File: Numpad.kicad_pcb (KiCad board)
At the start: 2 copper layers, 82.6 x 127 mm, 68 parts, among them J1 SWD, J2 USB_C_Receptacle_USB2.0, U1 SRV05-4, U2 STM32F103C8Tx, U3 XC6206PxxxMR, Y1 8MHz

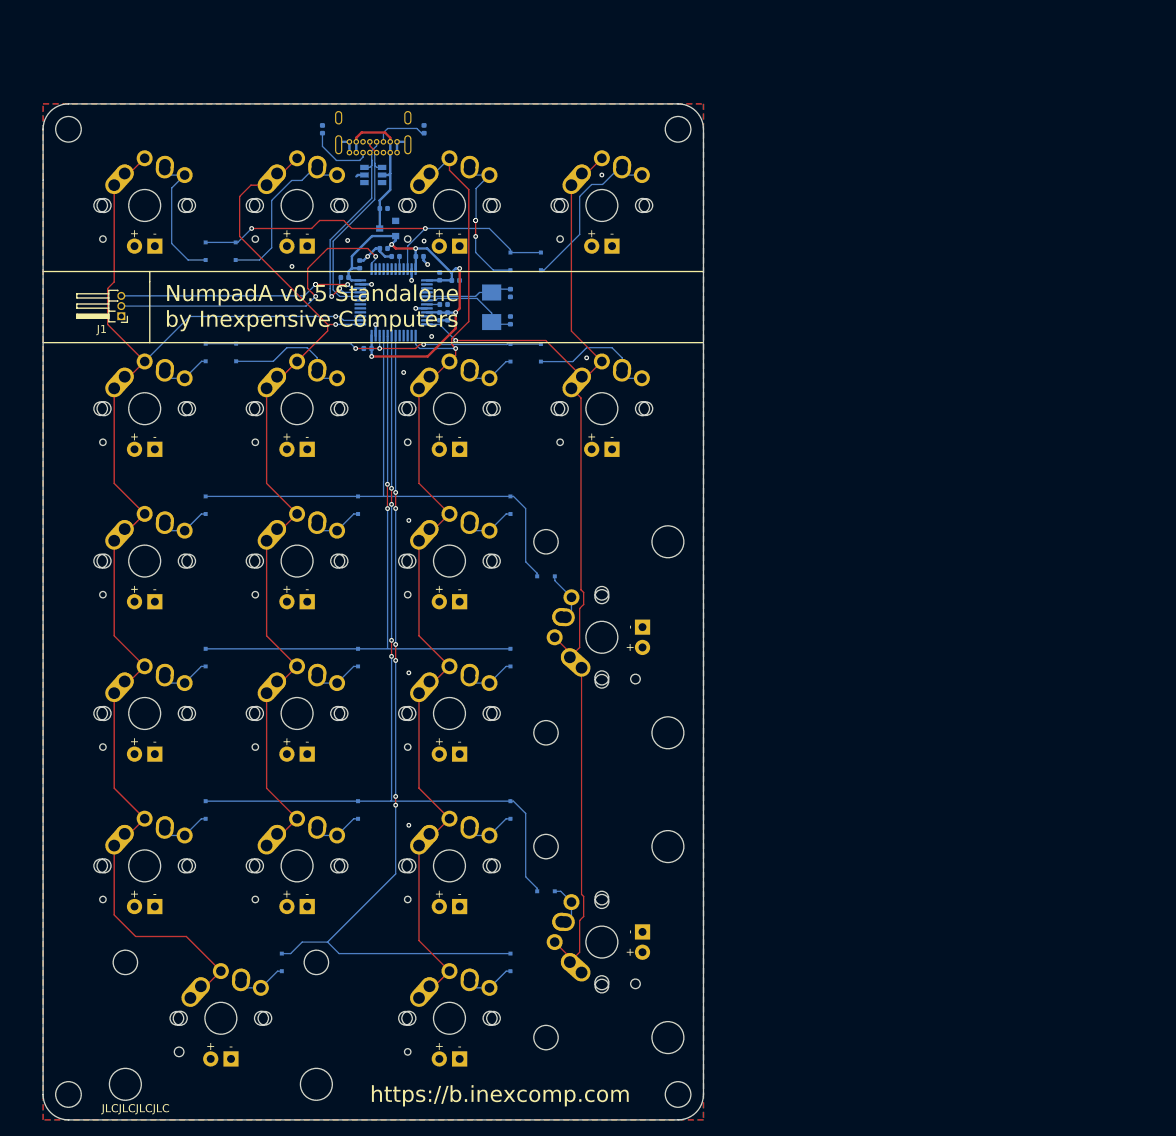
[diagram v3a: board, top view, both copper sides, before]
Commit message: Fixed header footprint
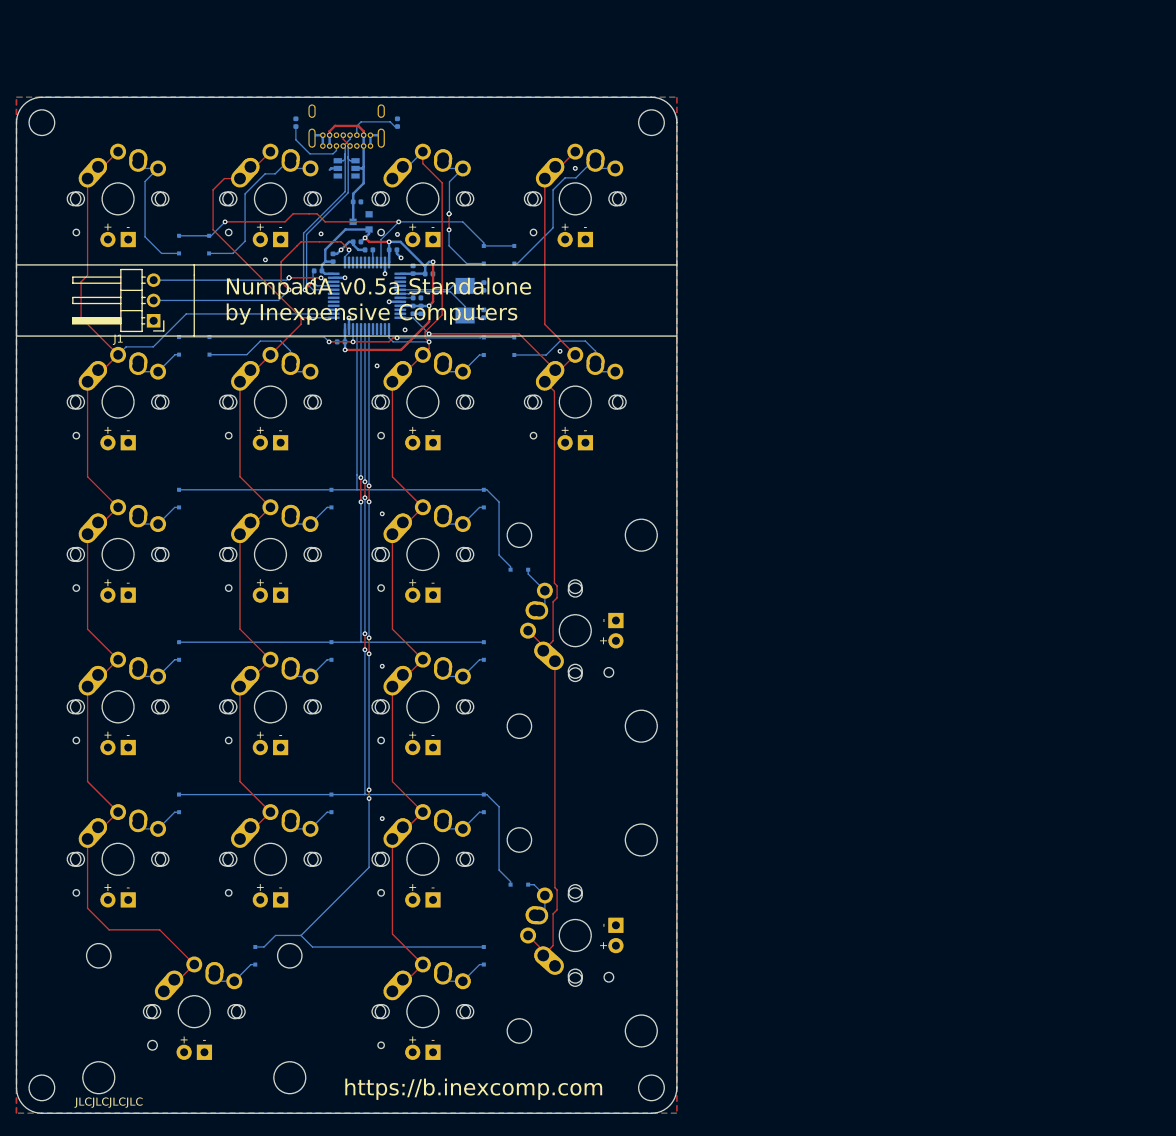
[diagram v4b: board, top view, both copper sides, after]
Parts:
- J1: footprint Connector_PinHeader_1.27mm:PinHeader_1x03_P1.27mm_Horizontal -> Connector_PinHeader_2.54mm:PinHeader_1x03_P2.54mm_Horizontal
- moved J1 4.08 mm to (55.2, 66.0)
- moved D_SLASH1 3.43 mm to (62.2, 69.2)
- moved C2 3.43 mm to (78.7, 68.7)
- moved C5 3.43 mm to (88.7, 64.7)
- moved C6 3.43 mm to (87.7, 64.7)
- moved C9 3.43 mm to (96.5, 65.2)
- moved D_0 3.43 mm to (67.9, 145.4)
- moved D_5 3.43 mm to (77.5, 107.3)
- moved D_6 3.43 mm to (96.5, 107.3)
- moved D_8 3.43 mm to (77.5, 88.3)
- moved D_9 3.43 mm to (96.5, 88.3)
- moved D_DOT1 3.43 mm to (96.5, 145.4)
- moved D_ENTER1 3.43 mm to (101.0, 136.5)
- moved D_MINUS1 3.43 mm to (100.3, 69.2)
- moved D_PLUS1 3.43 mm to (101.0, 97.2)
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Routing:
- net SWDIO: track 30.7 -> 22.8 mm
- net SWDCLK: track 40.4 -> 33.1 mm
- net col1: track 150.2 -> 149.8 mm, vias 1 -> 0
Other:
- board text added: "NumpadA v0.5a Standalone by Inexpensive Computers"
- board text removed: "NumpadA v0.5 Standalone by Inexpensive Computers"

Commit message: some changes; added license
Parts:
- removed J1: SWD, Connector_PinHeader_2.54mm:PinHeader_1x03_P2.54mm_Horizontal
- added GND1: TestPoint, TestPoint:TestPoint_Pad_D2.0mm, B.Cu at (65.1, 63.4)
- added SCK1: TestPoint, TestPoint:TestPoint_Pad_D2.0mm, B.Cu at (69.2, 63.4)
- added SIO1: TestPoint, TestPoint:TestPoint_Pad_D2.0mm, B.Cu at (73.2, 63.4)
- D_0, D_1, D_2, D_3, D_4, D_5, D_6, D_7, D_8, D_9, D_BKSP1, D_DOT1, D_ENTER1, D_ESC1, D_FN1, D_MINUS1, D_NUMLK1, D_PLUS1, D_SLASH1, D_STAR1, D_TAB1: value 1N4148 -> 1N4148WS; footprint Diode_SMD:D_SOD-323F -> Diode_SMD:D_SOD-323
- SW_0, SW_1, SW_2, SW_3, SW_4, SW_5, SW_6, SW_7, SW_8, SW_9, SW_BKSP1, SW_DOT1, SW_ENTER1, SW_ESC1, SW_FN1, SW_MINUS1, SW_NUMLK1, SW_PLUS1, SW_SLASH1, SW_STAR1, SW_TAB1: value SW_Push -> MX-LED
- moved C8 0.86 mm to (97.4, 61.6)
- moved D_0 0.86 mm to (68.8, 145.3)
- moved D_3 0.86 mm to (97.4, 126.2)
- moved D_DOT1 0.86 mm to (97.4, 145.3)
- moved D_STAR1 0.86 mm to (97.4, 69.1)
- moved H2 0.86 mm to (118.3, 41.1)
- moved H4 0.86 mm to (118.3, 161.8)
- moved R2 0.86 mm to (73.9, 41.1)
- moved R3 0.86 mm to (86.6, 41.1)
- moved SW_2 0.86 mm to (70.7, 133.2)
- moved SW_3 0.86 mm to (89.8, 133.2)
- moved SW_SLASH1 0.86 mm to (70.7, 76.0)
- moved SW_STAR1 0.86 mm to (89.8, 76.0)
- moved D_FN1 0.86 mm to (97.4, 57.6)
- moved R1 0.86 mm to (83.0, 57.0)
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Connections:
- SW_0 pad 3: (no net) -> LED_PWR
- SW_0 pad 4: (no net) -> GND
- SW_1 pad 3: (no net) -> LED_PWR
- SW_1 pad 4: (no net) -> GND
- SW_2 pad 3: (no net) -> LED_PWR
- SW_2 pad 4: (no net) -> GND
- SW_3 pad 3: (no net) -> LED_PWR
- SW_3 pad 4: (no net) -> GND
- SW_4 pad 3: (no net) -> LED_PWR
- SW_4 pad 4: (no net) -> GND
- SW_5 pad 3: (no net) -> LED_PWR
- SW_5 pad 4: (no net) -> GND
- SW_6 pad 3: (no net) -> LED_PWR
- SW_6 pad 4: (no net) -> GND
- SW_7 pad 3: (no net) -> LED_PWR
- SW_7 pad 4: (no net) -> GND
- SW_8 pad 3: (no net) -> LED_PWR
- SW_8 pad 4: (no net) -> GND
- SW_9 pad 3: (no net) -> LED_PWR
- SW_9 pad 4: (no net) -> GND
- SW_BKSP1 pad 3: (no net) -> LED_PWR
- SW_BKSP1 pad 4: (no net) -> GND
- SW_DOT1 pad 3: (no net) -> LED_PWR
- SW_DOT1 pad 4: (no net) -> GND
- SW_ENTER1 pad 3: (no net) -> LED_PWR
- SW_ENTER1 pad 4: (no net) -> GND
- SW_ESC1 pad 3: (no net) -> LED_PWR
- SW_ESC1 pad 4: (no net) -> GND
- SW_FN1 pad 3: (no net) -> LED_PWR
- SW_FN1 pad 4: (no net) -> GND
- SW_MINUS1 pad 3: (no net) -> LED_PWR
- SW_MINUS1 pad 4: (no net) -> GND
- SW_NUMLK1 pad 3: (no net) -> LED_PWR
- SW_NUMLK1 pad 4: (no net) -> GND
- SW_PLUS1 pad 3: (no net) -> LED_PWR
- SW_PLUS1 pad 4: (no net) -> GND
- SW_SLASH1 pad 3: (no net) -> LED_PWR
- SW_SLASH1 pad 4: (no net) -> GND
- SW_STAR1 pad 3: (no net) -> LED_PWR
- SW_STAR1 pad 4: (no net) -> GND
- SW_TAB1 pad 3: (no net) -> LED_PWR
- SW_TAB1 pad 4: (no net) -> GND
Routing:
- net SWDIO: track 22.8 -> 7.49 mm, vias 3 -> 2
- net SWDCLK: track 33.1 -> 18.3 mm
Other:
- outline, holes or cut-outs redrawn
- board text added: "NumpadA v0.6 Standalone by Inexpensive Computers"
- board text removed: "NumpadA v0.5a Standalone by Inexpensive Computers"

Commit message: v0.9pre
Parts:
- removed C1, C2, C3, C4, C6: 100nf, Capacitor_SMD:C_0402_1005Metric
- removed C5: 1uf, Capacitor_SMD:C_0402_1005Metric
- removed D_0, D_1, D_2, D_3, D_4, D_5, D_6, D_7, D_8, D_9, D_BKSP1, D_DOT1, D_ENTER1, D_ESC1, D_FN1, D_MINUS1, D_NUMLK1, D_PLUS1, D_SLASH1, D_STAR1, D_TAB1: 1N4148WS, Diode_SMD:D_SOD-323
- removed J2: USB_C_Receptacle_USB2.0, Connector_USB:USB_C_Receptacle_GCT_USB4085
- removed R4: 1.5K, Resistor_SMD:R_0402_1005Metric
- added C13: 20pf, Capacitor_SMD:C_0402_1005Metric, B.Cu at (80.6, 66.7)
- added C14: 100nf, Capacitor_SMD:C_0402_1005Metric, B.Cu at (81.3, 61.3)
- added C15: 100nf, Capacitor_SMD:C_0402_1005Metric, B.Cu at (87.6, 58.4)
- added C16: 1uf, Capacitor_SMD:C_0402_1005Metric, B.Cu at (79.4, 61.3)
- added C17: 100nf, Capacitor_SMD:C_0402_1005Metric, B.Cu at (80.3, 61.3)
- added C18: 100nf, Capacitor_SMD:C_0402_1005Metric, B.Cu at (77.5, 49.5)
- added D1: WS2813, LED_SMD:LED_WS2812_PLCC6_5.0x5.0mm_P1.6mm, B.Cu at (62.9, 53.3)
- added D10: BAT54C, Package_TO_SOT_SMD:SOT-23, B.Cu at (62.9, 101.0)
- added D11: BAT54C, Package_TO_SOT_SMD:SOT-23, B.Cu at (62.9, 115.6)
- added D12: BAT54C, Package_TO_SOT_SMD:SOT-23, B.Cu at (81.9, 139.7)
- added D13: BAT54C, Package_TO_SOT_SMD:SOT-23, B.Cu at (101.0, 43.8)
- added D14: BAT54C, Package_TO_SOT_SMD:SOT-23, B.Cu at (101.0, 60.3)
- added D15: BAT54C, Package_TO_SOT_SMD:SOT-23, B.Cu at (101.0, 77.5)
- added D16: BAT54C, Package_TO_SOT_SMD:SOT-23, B.Cu at (101.0, 101.0)
- added D17: BAT54C, Package_TO_SOT_SMD:SOT-23, B.Cu at (101.0, 115.6)
- added D2: WS2813, LED_SMD:LED_WS2812_PLCC6_5.0x5.0mm_P1.6mm, B.Cu at (99.1, 53.3)
- added D3: WS2813, LED_SMD:LED_WS2812_PLCC6_5.0x5.0mm_P1.6mm, B.Cu at (62.9, 92.7)
- added D4: WS2813, LED_SMD:LED_WS2812_PLCC6_5.0x5.0mm_P1.6mm, B.Cu at (99.1, 92.7)
- added D5: WS2813, LED_SMD:LED_WS2812_PLCC6_5.0x5.0mm_P1.6mm, B.Cu at (62.9, 130.2)
- added D6: WS2813, LED_SMD:LED_WS2812_PLCC6_5.0x5.0mm_P1.6mm, B.Cu at (99.1, 130.2)
- added D7: BAT54C, Package_TO_SOT_SMD:SOT-23, B.Cu at (62.9, 43.8)
- added D8: BAT54C, Package_TO_SOT_SMD:SOT-23, B.Cu at (62.9, 61.6)
- added D9: BAT54C, Package_TO_SOT_SMD:SOT-23, B.Cu at (62.9, 77.5)
- added F1: SMD0805P050TF, Fuse:Fuse_0805_2012Metric_Castellated, B.Cu at (83.8, 38.7)
- added G***: LOGO, Logo:inexcomplogo1, F.Cu at (53.3, 52.7)
- added G***: LOGO, Logo:OSHWMark, F.Cu at (109.2, 52.7)
- added J1: USB_C_Receptacle_USB2.0, Connector_USB:USB_C_Receptacle_HRO_TYPE-C-31-M-12, B.Cu at (81.9, 31.1)
- added Q1: AO3401A, Package_TO_SOT_SMD:SOT-23, B.Cu at (90.2, 51.4)
- added R11: 10k, Resistor_SMD:R_0402_1005Metric, B.Cu at (88.3, 55.2)
- added R12: 1.5K, Resistor_SMD:R_0402_1005Metric, B.Cu at (83.8, 46.0)
- added R13: 5.1K, Resistor_SMD:R_0402_1005Metric, B.Cu at (89.2, 34.6)
- added R14: 5.1K, Resistor_SMD:R_0402_1005Metric, B.Cu at (87.8, 34.6)
- C10, C7: value 100nf -> 1uf
- C11: value 1uf -> 100nf
- C12: value 1uf -> 20pf
- C8, C9: value 20pf -> 100nf
- R1: value 10k -> 10K
- R2: value 5.1K -> 150R
- R3: value 5.1K -> 1M
- SW_0, SW_ENTER1, SW_PLUS1: footprint Keebio-Parts:MX-Alps-Choc-2U -> Keebio-Parts:MX-Alps-Choc-2U-StabFlip
- U1: value SRV05-4 -> STM32F103C8Tx; footprint Package_TO_SOT_SMD:SOT-23-6 -> Package_QFP:LQFP-48_7x7mm_P0.5mm
- U2: value STM32F103C8Tx -> XC6206PxxxMR; footprint Package_QFP:LQFP-48_7x7mm_P0.5mm -> Package_TO_SOT_SMD:SOT-23
- U3: value XC6206PxxxMR -> SRV05-4; footprint Package_TO_SOT_SMD:SOT-23 -> Package_TO_SOT_SMD:SOT-23-6
- moved H3 159.9 mm to (139.4, 34.9)
- moved H4 120.8 mm to (139.4, 42.9)
- moved H1 89.5 mm to (131.4, 34.9)
- moved C9 25.0 mm to (76.8, 50.8), turned to 180 degrees
- moved R2 21.3 mm to (90.8, 54.0), turned to 180 degrees
- moved SIO1 18.4 mm to (57.8, 53.3), turned to 270 degrees
- moved U2 17.4 mm to (86.4, 45.7)
- moved C7 17.0 mm to (86.4, 43.5)
- moved C10 15.1 mm to (87.6, 47.9)
- moved GND1 15.1 mm to (57.8, 50.2), turned to 270 degrees
- moved R3 14.6 mm to (72.4, 37.5), turned to 180 degrees
- moved SCK1 13.3 mm to (57.8, 56.5), turned to 270 degrees
- moved H2 13.2 mm to (131.4, 42.9)
- moved Y1 13.1 mm to (81.9, 64.1), turned to 0 degrees
- moved C8 11.2 mm to (86.4, 59.7), turned to 180 degrees
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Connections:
- net LED_PWR renamed LED_MATRIX
- C10 pad 1: NRST -> VBAT
- C11 pad 2: +5V -> VBAT
- C12 pad 1: VBAT -> PD0
- C7 pad 2: VBAT -> +5V
- C8 pad 1: PD0 -> GND
- C8 pad 2: GND -> VBAT
- C9 pad 1: PD1 -> GND
- C9 pad 2: GND -> VBAT
- R1 pad 1: BOOT0 -> +5V
- R1 pad 2: GND -> LED_CONTROL
- R2 pad 1: /CC1 -> Net-(Q1-Pad1)
- R2 pad 2: GND -> LED_CONTROL
- R3 pad 1: GND -> Net-(J1-PadS1)
- R3 pad 2: /CC2 -> GND
- U1 pad 1: (no net) -> VBAT
- U1 pad 2: GND -> (no net)
- U1 pad 3: DA+ -> (no net)
- U1 pad 4: DA- -> (no net)
- U1 pad 5: +5V -> PD0
- U1 pad 6: (no net) -> PD1
- U2 pad 1: VBAT -> GND
- U2 pad 2: (no net) -> VBAT
- U2 pad 3: (no net) -> +5V
- U3 pad 1: GND -> (no net)
- U3 pad 2: VBAT -> GND
- U3 pad 3: +5V -> DA-
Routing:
- net GND: track 19.9 -> 541.1 mm, vias 16 -> 92
- net LED_MATRIX: track 0.00 -> 461.7 mm, vias 0 -> 26
- net +5V: track 19.6 -> 224.8 mm, vias 0 -> 15
- net Net-(D2-Pad4): track 0.00 -> 99.5 mm, vias 0 -> 8
- net Net-(D2-Pad6): track 0.00 -> 98.1 mm, vias 0 -> 10
- net Net-(D2-Pad3): track 0.00 -> 92.8 mm, vias 0 -> 9
- net Net-(D1-Pad3): track 0.00 -> 76.6 mm, vias 0 -> 4
- net BL_CONTROL: track 0.00 -> 57.9 mm, vias 0 -> 5
- net Net-(D4-Pad3): track 0.00 -> 46.0 mm, vias 0 -> 4
- net row2: track 44.0 -> 72.4 mm, vias 3 -> 8
- net col3: track 122.9 -> 149.0 mm, vias 1 -> 5
- net Net-(J1-PadS1): track 0.00 -> 24.1 mm
- net row4: track 77.3 -> 101.3 mm, vias 2 -> 12
- net SWDIO: track 7.49 -> 30.0 mm
- net SWDCLK: track 18.3 -> 40.0 mm, vias 2 -> 4
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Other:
- board size 82.6 x 127 mm -> 71.1 x 120.6 mm
- board text added: "NumpadA v0.9 Standalone by Inexpensive Computers"
- board text removed: "NumpadA v0.6 Standalone by Inexpensive Computers"

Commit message: v0.9
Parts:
- removed C14, C17: 100nf, Capacitor_SMD:C_0402_1005Metric
- removed C16: 1uf, Capacitor_SMD:C_0402_1005Metric
- removed the C9 at (76.8, 50.8)
- removed the D12 at (81.9, 139.7)
- removed the D13 at (101.0, 43.8)
- removed H1, H2, H3, H4: MountingHole, MountingHole:MountingHole_3.2mm_M3
- removed the U3 at (81.9, 43.2)
- added C1: 1uf, Capacitor_SMD:C_0402_1005Metric, B.Cu at (86.4, 43.5)
- added C10: 1uf, Capacitor_SMD:C_0402_1005Metric, B.Cu at (79.4, 61.3)
- added C12: 100nf, Capacitor_SMD:C_0402_1005Metric, B.Cu at (80.3, 61.3)
- added C5: 100nf, Capacitor_SMD:C_0402_1005Metric, B.Cu at (81.3, 61.3)
- added D3: BAT54C, Package_TO_SOT_SMD:SOT-23, B.Cu at (62.9, 59.1)
- added D7: BAT54C, Package_TO_SOT_SMD:SOT-23, B.Cu at (62.9, 100.3)
- added R1: 470R, Resistor_SMD:R_0805_2012Metric, B.Cu at (53.3, 48.3)
- added R10: 470R, Resistor_SMD:R_0805_2012Metric, B.Cu at (72.4, 92.7)
- added R12: 470R, Resistor_SMD:R_0805_2012Metric, B.Cu at (111.1, 103.5)
- added R13: 470R, Resistor_SMD:R_0805_2012Metric, B.Cu at (53.3, 111.8)
- added R15: 470R, Resistor_SMD:R_0805_2012Metric, B.Cu at (91.4, 111.8)
- added R17: 470R, Resistor_SMD:R_0805_2012Metric, B.Cu at (57.1, 132.1)
- added R18: 470R, Resistor_SMD:R_0805_2012Metric, B.Cu at (68.6, 132.1)
- added R19: 470R, Resistor_SMD:R_0805_2012Metric, B.Cu at (91.4, 130.8)
- added R2: 470R, Resistor_SMD:R_0805_2012Metric, B.Cu at (72.4, 48.3)
- added R20: 470R, Resistor_SMD:R_0805_2012Metric, B.Cu at (111.1, 141.6)
- added R21: 470R, Resistor_SMD:R_0805_2012Metric, B.Cu at (53.3, 142.9)
- added R22: 470R, Resistor_SMD:R_0805_2012Metric, B.Cu at (81.9, 142.9)
- added R28: 10k, Resistor_SMD:R_0402_1005Metric, B.Cu at (88.9, 55.6)
- added R29: 5.1K, Resistor_SMD:R_0402_1005Metric, B.Cu at (87.8, 34.6)
- added R3: 470R, Resistor_SMD:R_0805_2012Metric, B.Cu at (96.5, 43.8)
- added R4: 470R, Resistor_SMD:R_0805_2012Metric, B.Cu at (110.5, 48.3)
- added R5: 470R, Resistor_SMD:R_0805_2012Metric, B.Cu at (53.3, 73.7)
- added R6: 470R, Resistor_SMD:R_0805_2012Metric, B.Cu at (72.4, 73.7)
- added R7: 470R, Resistor_SMD:R_0805_2012Metric, B.Cu at (91.4, 73.7)
- added R8: 470R, Resistor_SMD:R_0805_2012Metric, B.Cu at (110.5, 73.7)
- added R9: 470R, Resistor_SMD:R_0805_2012Metric, B.Cu at (53.3, 92.7)
- added U1: XC6206PxxxMR, Package_TO_SOT_SMD:SOT-23, B.Cu at (86.4, 45.7)
- C7: value 1uf -> 100nf
- D14, D15, D16, D17: value BAT54C -> WS2813; footprint Package_TO_SOT_SMD:SOT-23 -> LED_SMD:LED_WS2812_PLCC6_5.0x5.0mm_P1.6mm
- D2, D4, D5, D6: value WS2813 -> BAT54C; footprint LED_SMD:LED_WS2812_PLCC6_5.0x5.0mm_P1.6mm -> Package_TO_SOT_SMD:SOT-23
- R11: value 10k -> 470R; footprint Resistor_SMD:R_0402_1005Metric -> Resistor_SMD:R_0805_2012Metric
- R14: value 5.1K -> 470R; footprint Resistor_SMD:R_0402_1005Metric -> Resistor_SMD:R_0805_2012Metric
- U2: value XC6206PxxxMR -> SRV05-4; footprint Package_TO_SOT_SMD:SOT-23 -> Package_TO_SOT_SMD:SOT-23-6
- moved R14 78.7 mm to (72.4, 111.8), turned to 0 degrees
- moved D15 65.5 mm to (62.9, 130.8), turned to 90 degrees
- moved D6 52.7 mm to (101.0, 77.5), turned to 90 degrees
- moved D5 52.7 mm to (62.9, 77.5)
- moved D16 47.7 mm to (99.1, 53.3)
- moved D10 40.8 mm to (101.0, 115.6), turned to 90 degrees
- moved D8 39.8 mm to (81.9, 96.5), turned to 90 degrees
- moved D9 38.1 mm to (62.9, 115.6), turned to 90 degrees
- moved R11 37.6 mm to (91.4, 92.7)
- moved D14 32.8 mm to (99.1, 93.0), turned to 90 degrees
- moved D4 29.9 mm to (101.0, 62.9)
- moved D11 26.9 mm to (81.9, 134.6), turned to 90 degrees
- moved D17 15.4 mm to (99.1, 130.8), turned to 90 degrees
- moved C7 12.0 mm to (76.8, 50.8)
- moved R26 7.47 mm to (79.7, 39.1), turned to 0 degrees
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- renumbered C18 to C11, C10 to C2, C12 to C3, C13 to C4, C8 to C6, C11 to C8, C15 to C9, D7 to D1, D1 to D12, D3 to D13, R1 to R23, R2 to R24, R12 to R25, R3 to R26, R13 to R27, SW_7 to SW_1, SW_0 to SW_10, SW_8 to SW_2, SW_9 to SW_3, SW_1 to SW_7, SW_2 to SW_8, SW_3 to SW_9, U1 to U3
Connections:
- C7 pad 2: +5V -> VBAT
- D10 pad 3: row4 -> row5
- D11 pad 3: row5 -> row6
- D12 pad 1: (no net) -> Net-(D12-Pad1)
- D12 pad 3: Net-(D1-Pad3) -> Net-(D12-Pad3)
- D13 pad 1: (no net) -> Net-(D13-Pad1)
- D13 pad 3: Net-(D2-Pad6) -> Net-(D13-Pad3)
- D13 pad 4: Net-(D1-Pad3) -> Net-(D12-Pad3)
- D14 pad 2: Net-(D14-Pad2) -> +5V
- D14 pad 3: row2 -> Net-(D14-Pad3)
- D15 pad 2: Net-(D15-Pad2) -> +5V
- D15 pad 3: row3 -> Net-(D15-Pad3)
- D16 pad 2: (no net) -> +5V
- D16 pad 3: row4 -> Net-(D16-Pad3)
- D17 pad 2: Net-(D17-Pad2) -> +5V
- D17 pad 3: row5 -> Net-(D17-Pad3)
- D2 pad 1: (no net) -> Net-(D2-Pad1)
- D2 pad 2: +5V -> Net-(D2-Pad2)
- D2 pad 3: Net-(D2-Pad3) -> row1
- D4 pad 1: (no net) -> Net-(D4-Pad1)
- D4 pad 2: +5V -> Net-(D4-Pad2)
- D4 pad 3: Net-(D4-Pad3) -> row2
- D5 pad 1: (no net) -> Net-(D5-Pad1)
- D5 pad 2: +5V -> Net-(D5-Pad2)
- D5 pad 3: Net-(D2-Pad4) -> row3
- D6 pad 1: (no net) -> Net-(D6-Pad1)
- D6 pad 2: +5V -> Net-(D6-Pad2)
- D6 pad 3: (no net) -> row3
- D8 pad 3: row2 -> row4
- D9 pad 3: row3 -> row5
- J1 pad A8: (no net) -> Net-(J1-PadA8)
- J1 pad B8: (no net) -> Net-(J1-PadB8)
- R11 pad 1: BOOT0 -> Net-(R11-Pad1)
- R11 pad 2: GND -> LED_MATRIX
- R14 pad 1: GND -> Net-(R14-Pad1)
- R14 pad 2: /MCUSupport/CC2 -> LED_MATRIX
- SW_1 pad 2: Net-(D9-Pad1) -> Net-(D5-Pad2)
- SW_1 pad 3: LED_MATRIX -> Net-(R9-Pad1)
- SW_10 pad 2: Net-(D12-Pad1) -> Net-(D11-Pad2)
- SW_10 pad 3: LED_MATRIX -> Net-(R21-Pad1)
- SW_2 pad 2: Net-(D9-Pad2) -> Net-(D5-Pad1)
- SW_2 pad 3: LED_MATRIX -> Net-(R10-Pad1)
- SW_3 pad 2: Net-(D15-Pad1) -> Net-(D6-Pad2)
- SW_3 pad 3: LED_MATRIX -> Net-(R11-Pad1)
- SW_4 pad 2: Net-(D10-Pad1) -> Net-(D7-Pad2)
- SW_4 pad 3: LED_MATRIX -> Net-(R13-Pad1)
- SW_5 pad 2: Net-(D10-Pad2) -> Net-(D7-Pad1)
- SW_5 pad 3: LED_MATRIX -> Net-(R14-Pad1)
- SW_6 pad 2: Net-(D16-Pad1) -> Net-(D8-Pad1)
- SW_6 pad 3: LED_MATRIX -> Net-(R15-Pad1)
- SW_7 pad 2: Net-(D11-Pad1) -> Net-(D9-Pad2)
- SW_7 pad 3: LED_MATRIX -> Net-(R17-Pad1)
- SW_8 pad 2: Net-(D11-Pad2) -> Net-(D9-Pad1)
- SW_8 pad 3: LED_MATRIX -> Net-(R18-Pad1)
- SW_9 pad 2: Net-(D17-Pad1) -> Net-(D10-Pad2)
- SW_9 pad 3: LED_MATRIX -> Net-(R19-Pad1)
- SW_BKSP1 pad 2: Net-(D13-Pad2) -> Net-(D2-Pad2)
- SW_BKSP1 pad 3: LED_MATRIX -> Net-(R4-Pad1)
- SW_DOT1 pad 2: Net-(D12-Pad2) -> Net-(D11-Pad1)
- SW_DOT1 pad 3: LED_MATRIX -> Net-(R22-Pad1)
- SW_ENTER1 pad 2: Net-(D17-Pad2) -> Net-(D10-Pad1)
- SW_ENTER1 pad 3: LED_MATRIX -> Net-(R20-Pad1)
- SW_ESC1 pad 3: LED_MATRIX -> Net-(R1-Pad1)
- SW_FN1 pad 2: Net-(D13-Pad1) -> Net-(D2-Pad1)
- SW_FN1 pad 3: LED_MATRIX -> Net-(R3-Pad1)
- SW_MINUS1 pad 2: Net-(D14-Pad2) -> Net-(D4-Pad2)
- SW_MINUS1 pad 3: LED_MATRIX -> Net-(R8-Pad1)
- SW_NUMLK1 pad 2: Net-(D8-Pad1) -> Net-(D3-Pad2)
- SW_NUMLK1 pad 3: LED_MATRIX -> Net-(R5-Pad1)
- SW_PLUS1 pad 2: Net-(D15-Pad2) -> Net-(D6-Pad1)
- SW_PLUS1 pad 3: LED_MATRIX -> Net-(R12-Pad1)
- SW_SLASH1 pad 2: Net-(D8-Pad2) -> Net-(D3-Pad1)
- SW_SLASH1 pad 3: LED_MATRIX -> Net-(R6-Pad1)
- SW_STAR1 pad 2: Net-(D14-Pad1) -> Net-(D4-Pad1)
- SW_STAR1 pad 3: LED_MATRIX -> Net-(R7-Pad1)
- SW_TAB1 pad 3: LED_MATRIX -> Net-(R2-Pad1)
- U2 pad 1: GND -> Net-(U2-Pad1)
- U2 pad 2: VBAT -> GND
- U2 pad 3: +5V -> DA-
- U3 pad 10: (no net) -> Net-(U3-Pad10)
- U3 pad 11: (no net) -> LED_NUMLK
- U3 pad 12: col4 -> Net-(U3-Pad12)
- U3 pad 13: col3 -> Net-(U3-Pad13)
- U3 pad 14: (no net) -> Net-(U3-Pad14)
- U3 pad 2: (no net) -> col4
- U3 pad 21: row1 -> Net-(U3-Pad21)
- U3 pad 22: (no net) -> Net-(U3-Pad22)
- U3 pad 27: (no net) -> Net-(U3-Pad27)
- U3 pad 28: (no net) -> Net-(U3-Pad28)
- U3 pad 29: (no net) -> Net-(U3-Pad29)
- U3 pad 3: (no net) -> col3
- U3 pad 30: (no net) -> Net-(U3-Pad30)
- U3 pad 31: (no net) -> Net-(U3-Pad31)
- U3 pad 38: (no net) -> row1
- U3 pad 39: (no net) -> Net-(U3-Pad39)
- U3 pad 4: (no net) -> Net-(U3-Pad4)
- U3 pad 40: (no net) -> Net-(U3-Pad40)
- U3 pad 41: (no net) -> Net-(U3-Pad41)
- U3 pad 43: (no net) -> Net-(U3-Pad43)
- U3 pad 45: (no net) -> Net-(U3-Pad45)
- U3 pad 46: (no net) -> Net-(U3-Pad46)
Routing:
- net Net-(D15-Pad3): track 0.00 -> 124.4 mm, vias 0 -> 2
- net Net-(D14-Pad3): track 0.00 -> 109.2 mm, vias 0 -> 4
- net Net-(D2-Pad4): track 99.5 -> 0.00 mm, vias 8 -> 0
- net Net-(D2-Pad6): track 98.1 -> 0.00 mm, vias 10 -> 0
- net Net-(D2-Pad3): track 92.8 -> 0.00 mm, vias 9 -> 0
- net Net-(D16-Pad3): track 0.00 -> 87.2 mm, vias 0 -> 5
- net Net-(D12-Pad3): track 0.00 -> 80.0 mm, vias 0 -> 4
- net Net-(D13-Pad3): track 0.00 -> 76.9 mm, vias 0 -> 3
- net Net-(D1-Pad3): track 76.6 -> 0.00 mm, vias 4 -> 0
- net Net-(D4-Pad3): track 46.0 -> 0.00 mm, vias 4 -> 0
- net LED_MATRIX: track 461.7 -> 430.4 mm, vias 26 -> 36
- net Net-(D15-Pad2): track 21.7 -> 0.00 mm, vias 1 -> 0
- net row1: track 68.3 -> 46.8 mm, vias 8 -> 3
- net row4: track 101.3 -> 80.6 mm, vias 12 -> 4
- net Net-(D2-Pad2): track 0.00 -> 19.9 mm, vias 0 -> 1
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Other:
- board size 71.1 x 120.6 mm -> 71.1 x 120.9 mm
- board text added: "GND"
- board text added: "NumpadA v0.9"
- board text added: "SCK"
- board text added: "SIO"
- board text added: "by Inexpensive Computers"
- board text removed: "NumpadA v0.9 Standalone by Inexpensive Computers"
